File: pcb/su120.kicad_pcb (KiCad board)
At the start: 2 copper layers, 98.8 x 98 mm, 341 parts, among them J1 MJ-4PP-9, J2 Conn_01x03, J3 Conn_01x08, J4 Conn_01x08, J5 Conn_01x03, J6 MJ-4PP-9, SW1 SW_Push, SW10 SW_Push, SW11 SW_Push, SW12 SW_Push, SW13 SW_Push, SW14 SW_Push, SW15 SW_Push, SW16 SW_Push, SW17 SW_Push, SW18 SW_Push, SW19 Rotary_Encoder_Switch, SW2 SW_Push, SW20 Rotary_Encoder_Switch, SW21 SW_Push, SW3 SW_Push, SW4 SW_Push, SW5 SW_Push, SW6 SW_Push, SW7 SW_Push, SW8 SW_Push, SW9 SW_Push, U1 ProMicro

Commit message: Rev.7
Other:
- board text added: "SU120 "YAKITORI" Rev.7 by @e3w2q"
- board text removed: "SU120 "YAKITORI" Rev.6 by @e3w2q"

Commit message: Rev.8
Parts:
- removed H51, H52, H53, H54, H55, H56: MountingHole_Pad, #footprint:1pin_conn
- added ?: , #footprint:M1.4_tapping_Hole_rev2, F.Cu at (77.8, 59.5)
- added ?: , #footprint:OLED_Hole, F.Cu at (78.6, 66.7)
- added ?: , #footprint:M1.4_tapping_Hole_rev2, F.Cu at (82.5, 59.5)
- added ?: , #footprint:M1.4_tapping_Hole_rev2, F.Cu at (82.5, 73.8)
- added ?: , #footprint:M1.4_tapping_Hole_rev2, F.Cu at (77.8, 73.8)
- added H57: MountingHole_Pad, #footprint:1pin_conn, F.Cu at (54.3, 69.1)
- added J7: Conn_02x05_Odd_Even, #footprint:IDC-Header_2x05_P2.54mm_Vertical, F.Cu at (108.7, 63.9)
- added J8: Conn_02x05_Odd_Even, #footprint:IDC-Header_2x05_P2.54mm_Vertical, F.Cu at (127.8, 63.9)
- ? (x148): footprint #footprint:M1.4_tapping_Hole -> #footprint:M1.4_tapping_Hole_rev2
- D1, D10, D11, D12, D13, D14, D15, D16, D17, D18, D19, D2, D20, D3, D4, D5, D6, D7, D8, D9: footprint #footprint:diode_TH_SMD -> #footprint:diode_TH_SMD_rev2
- moved SW18 0.12 mm to (83.7, 64.5)
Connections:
- J1 pad A: (no net) -> Net-(J1-PadA)
- J6 pad A: (no net) -> Net-(J6-PadA)
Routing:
- net GND: track 1034.3 -> 1077.7 mm, vias 124 -> 131
- net dummydata: track 54.4 -> 77.3 mm
- net X7: track 65.1 -> 84.2 mm, vias 2 -> 3
- net X4: track 184.3 -> 165.1 mm
- net X8: track 78.4 -> 95.2 mm, vias 1 -> 4
- net Y6: track 91.7 -> 88.6 mm
- net reset2: track 40.7 -> 43.7 mm, vias 0 -> 1
- net X9: track 72.8 -> 75.2 mm
- net Y2: track 266.4 -> 264.2 mm
- net reset1: track 52.1 -> 50.1 mm, vias 3 -> 2
- net data: track 55.1 -> 56.5 mm
- net Y1: track 234.4 -> 235.2 mm
- net dummyVCC: track 57.8 -> 57.0 mm, vias 1 -> 5
- net X3: track 103.1 -> 103.9 mm
- net X10: track 73.2 -> 73.8 mm
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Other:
- board text added: "SU120 "YAKITORI" Rev.8 by @e3w2q"
- board text removed: "SU120 "YAKITORI" Rev.7 by @e3w2q"

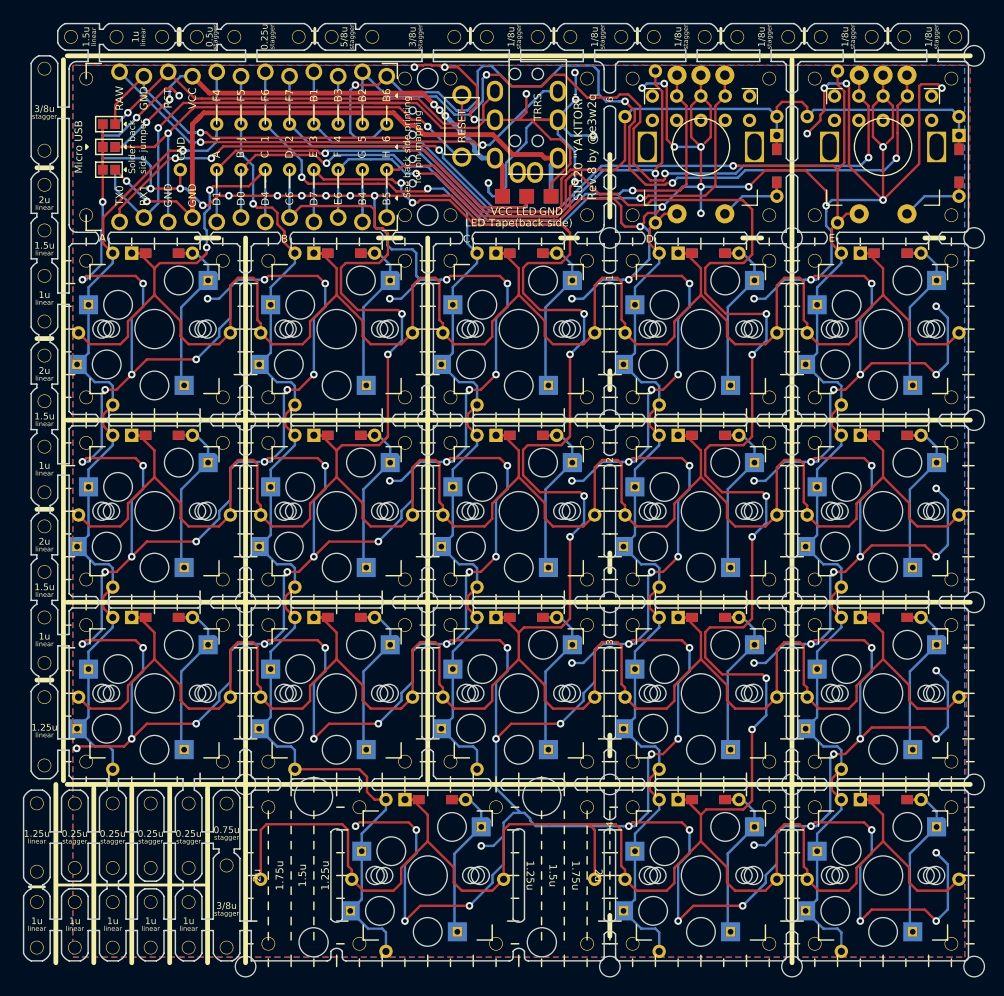
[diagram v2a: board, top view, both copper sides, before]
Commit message: adjust silk and hole size
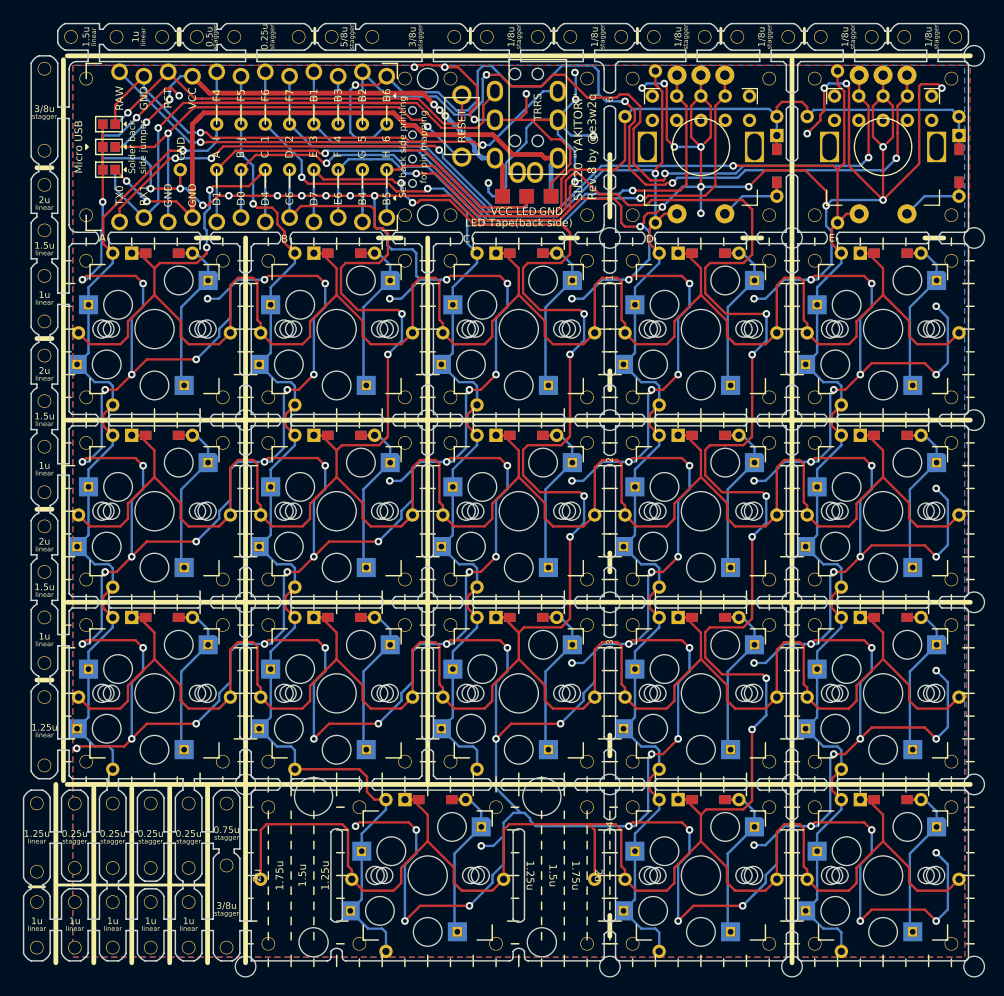
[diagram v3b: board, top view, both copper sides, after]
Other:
- board text added: "See back side printing"
- board text added: "for pin mapping"
- board text removed: "See back side printing for pin mapping"
